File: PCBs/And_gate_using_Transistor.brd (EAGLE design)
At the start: 29.5 x 34.5 mm, 11 parts, among them T1 BC547, T2 BC547

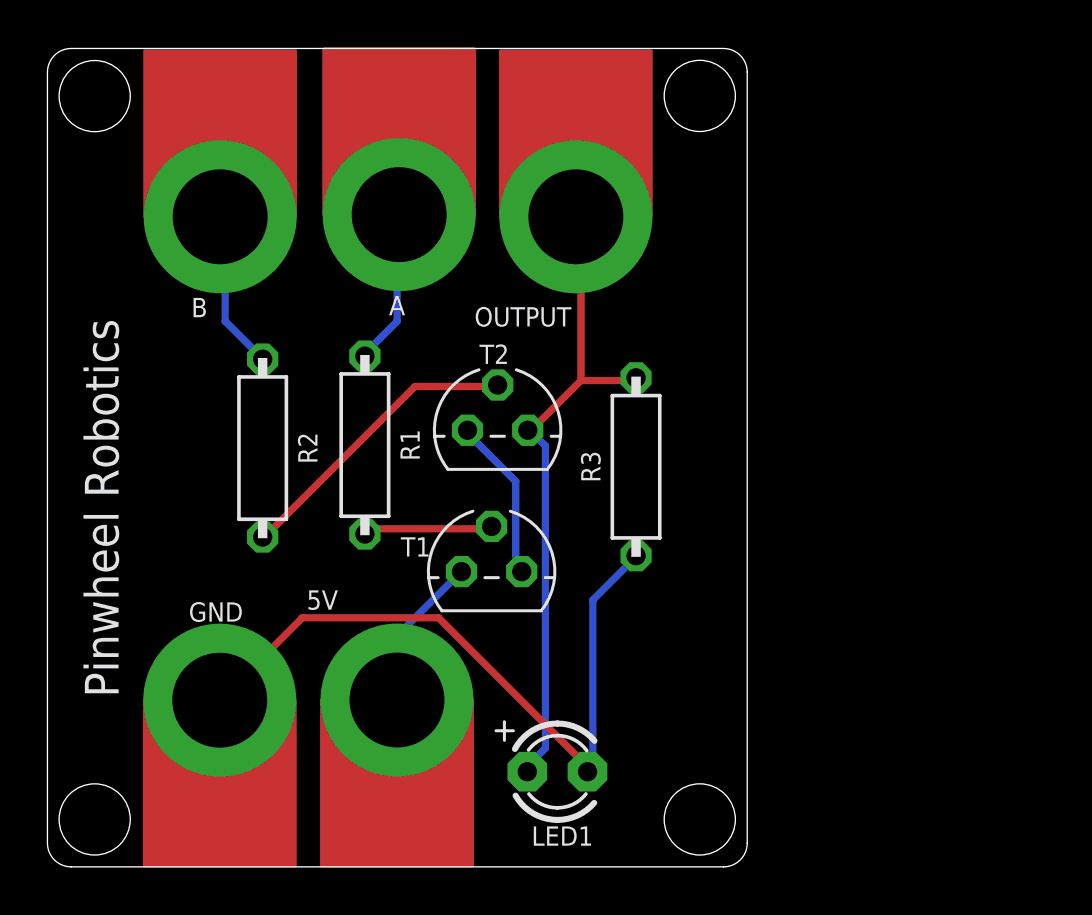
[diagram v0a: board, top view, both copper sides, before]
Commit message: Update for Dim width is 42 length is 28 for type 2 pcb
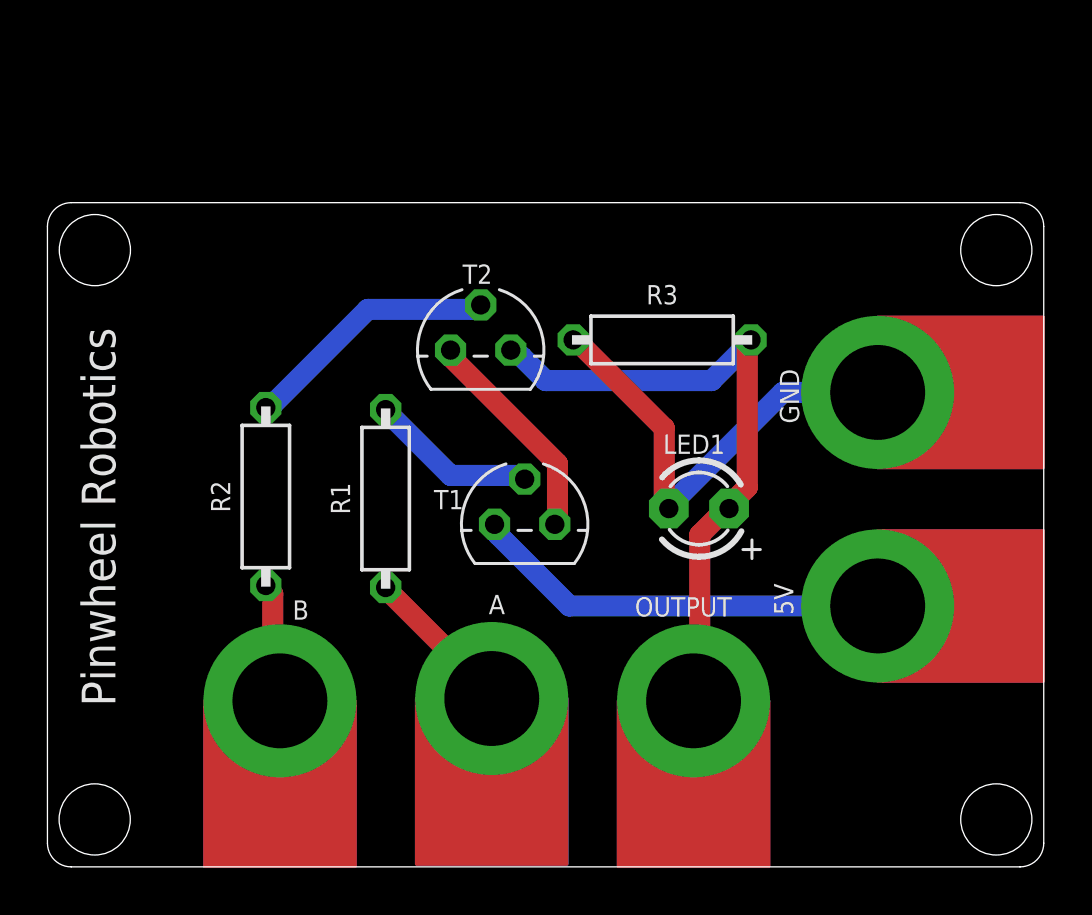
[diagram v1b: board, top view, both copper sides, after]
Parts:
- moved GND 30.6 mm to (35.0, 20.0), turned to 90 degrees
- moved OUTPUT 21.0 mm to (27.2, 7.00), turned to 0 degrees
- moved A 20.8 mm to (18.7, 7.10), turned to 0 degrees
- moved 5V 20.6 mm to (35.0, 11.0), turned to 90 degrees
- moved B 20.6 mm to (9.80, 7.00), turned to 0 degrees
- moved LED1 12.6 mm to (27.5, 15.1), turned to 180 degrees
- moved R3 5.46 mm to (25.9, 22.2), turned to 0 degrees
- moved T2 3.45 mm to (18.3, 21.8)
- moved T1 2.43 mm to (20.1, 14.4)
- moved R1 2.42 mm to (14.3, 15.5), turned to 90 degrees
- moved R2 2.05 mm to (9.21, 15.6), turned to 90 degrees
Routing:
- net 5V: track 6.54 -> 17.7 mm
- net GND: track 29.7 -> 19.7 mm
- net N$2: track 6.90 -> 9.28 mm
- net N$1: track 12.5 -> 10.8 mm
- net N$4: track 5.50 -> 7.10 mm
- net N$7: track 6.76 -> 5.27 mm
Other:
- board size 29.5 x 34.5 mm -> 42 x 28 mm

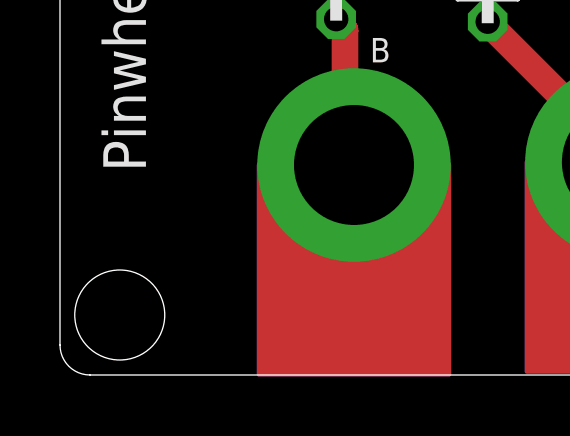
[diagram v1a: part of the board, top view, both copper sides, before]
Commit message: Corrected hole position for some design , made transistor as switch as category 1
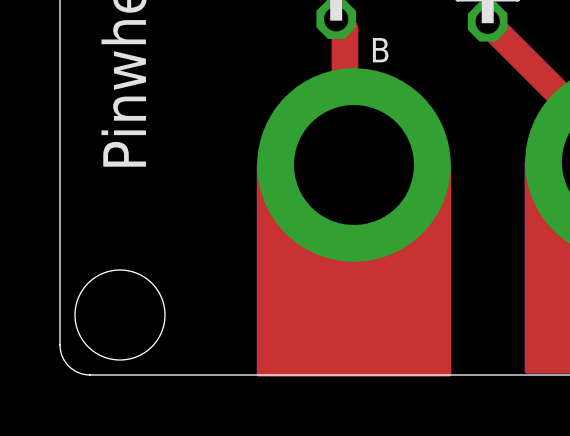
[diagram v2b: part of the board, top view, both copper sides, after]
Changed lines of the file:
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@@
 <drawing>
 <settings>
-<setting alwaysvectorfont="yes"/>
+<setting alwaysvectorfont="no"/>
 <setting verticaltext="up"/>
 </settings>
@@
 <wire x1="41" y1="28" x2="1" y2="28" width="0" layer="20"/>
 <wire x1="1" y1="28" x2="0" y2="27" width="0" layer="20" curve="90"/>
-<hole x="1.992" y="2" drill="3"/>
+<hole x="2" y="2" drill="3"/>
 <hole x="40" y="2" drill="3"/>
 <hole x="40" y="26" drill="3"/>
